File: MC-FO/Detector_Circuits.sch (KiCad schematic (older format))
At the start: 10 parts, among them U141 IFD97, U142 TLV3501AID, U143 74LVC1G32SE-7, U144 74LVC1G0832DBVT

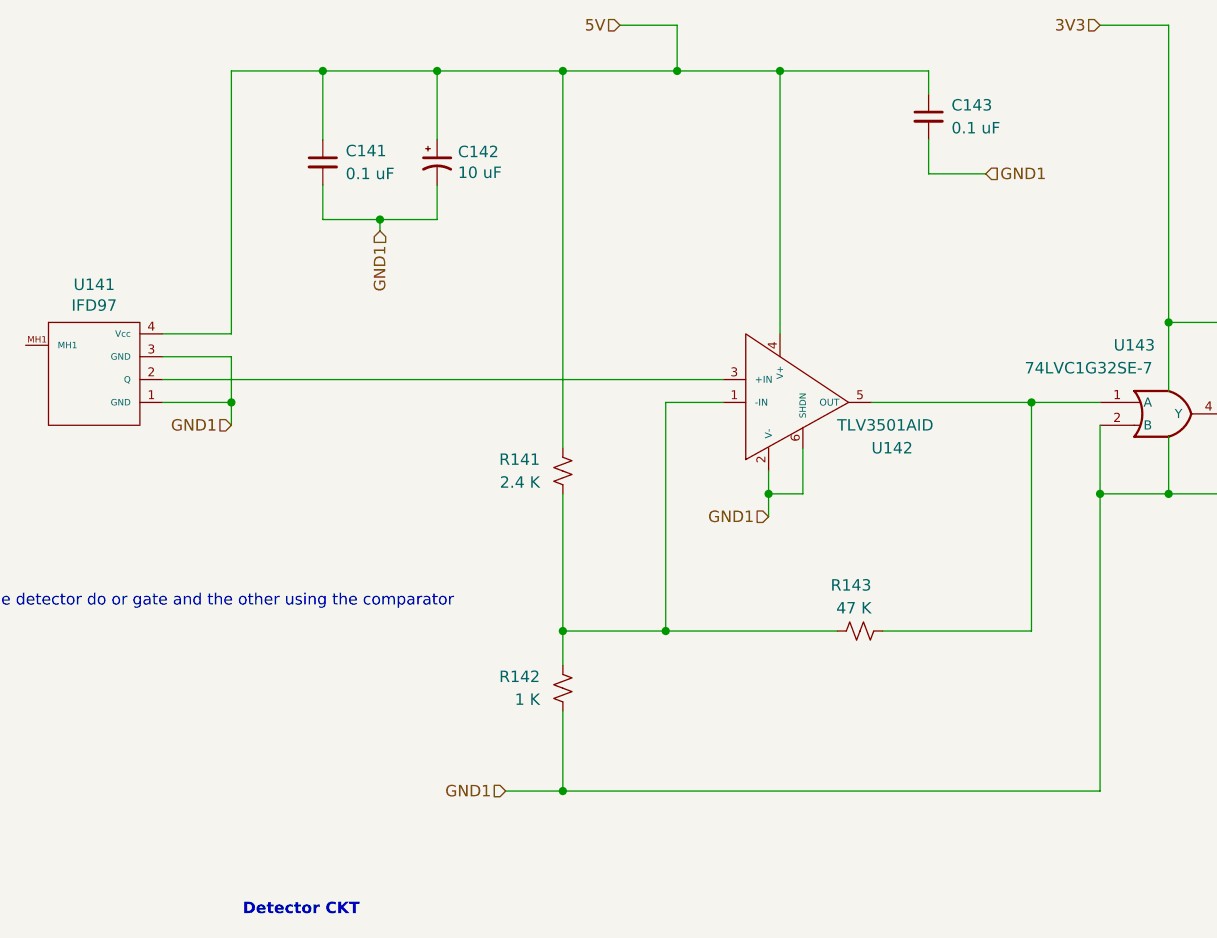
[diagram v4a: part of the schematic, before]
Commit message: changed status1 to output of detector
reassigned footprint of 550 LED
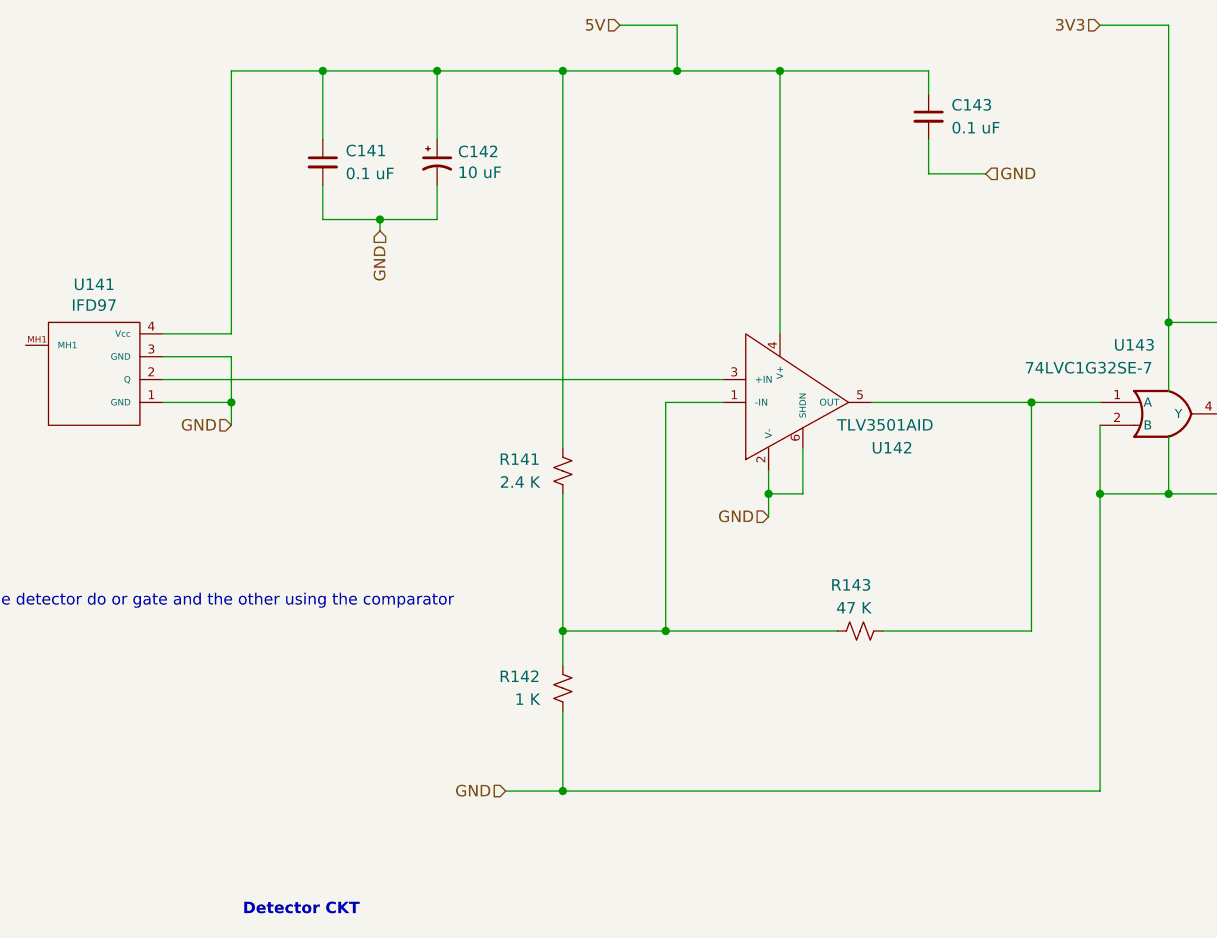
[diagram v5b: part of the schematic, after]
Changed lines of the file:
@@
 Connection ~ 7800 3650
 Text HLabel 5500 5350 0    50   Input ~ 0
-GND1
+GND
 Text HLabel 6650 4150 0    50   Input ~ 0
-GND1
+GND
 Text HLabel 4950 2900 3    50   Input ~ 0
-GND1
+GND
 Text HLabel 4300 3750 0    50   Input ~ 0
-GND1
+GND
 Text HLabel 7600 2650 2    50   Input ~ 0
-GND1
+GND
 Wire Wire Line
 	4700 2850 4950 2850

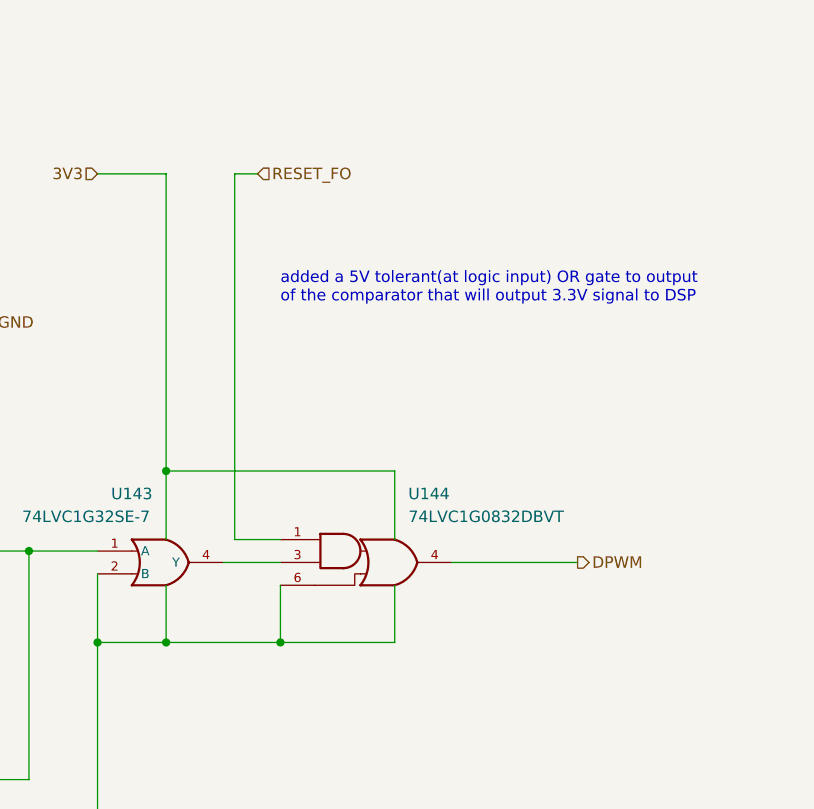
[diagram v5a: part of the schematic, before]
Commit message: Removed AND-OR gates
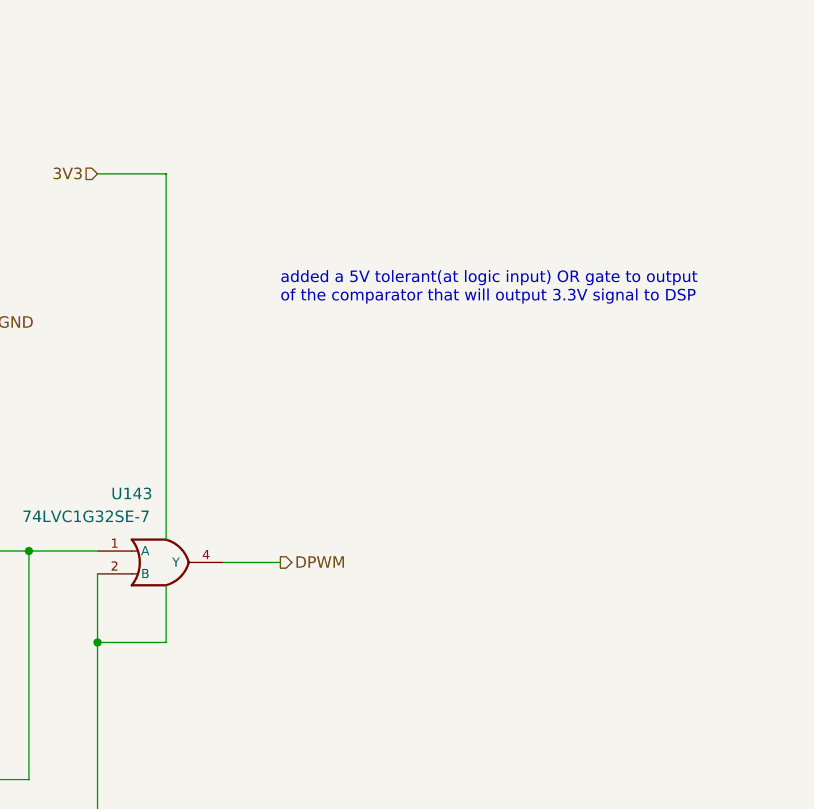
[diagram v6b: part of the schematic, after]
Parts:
- removed U144: 74LVC1G0832DBVT, Package_TO_SOT_SMD:SOT-23-6, symbol Existing_IC_Models:74LVC1G0832DBVT
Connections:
- net DPWM: now also U143.4 (Y)
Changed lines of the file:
@@
 	1    0    0    -1
 $EndComp
-Text HLabel 10200 3700 2    50   Output ~ 0
+Text HLabel 8900 3700 2    50   Output ~ 0
 DPWM
 Text HLabel 6000 2000 0    50   Input ~ 0
@@
 Text Notes 3100 4550 0    50   ~ 0
 on one detector do or gate and the other using the comparator
-Text HLabel 8800 2000 2    50   Input ~ 0
-RESET_FO
 $Comp
 L Existing_IC_Models:74LVC1G32SE-7 U143
@@
 	8100 5350 5750 5350
 Connection ~ 5750 5350
-Wire Wire Line
-	8400 3600 8400 3300
 Text HLabel 8100 2000 0    50   Input ~ 0
 3V3
@@
 added a 5V tolerant(at logic input) OR gate to output\nof the comparator that will output 3.3V signal to DSP\n\n
 Wire Wire Line
-	8800 2000 8700 2000
+	8900 3700 8650 3700
 Wire Wire Line
-	8700 2000 8700 3600
-Wire Wire Line
-	8700 3600 8900 3600
-Wire Wire Line
-	8900 3700 8650 3700
-Connection ~ 8400 3300
-Wire Wire Line
-	8400 3300 8400 2000
-Wire Wire Line
-	9650 3700 10200 3700
-$Comp
-L Existing_IC_Models:74LVC1G0832DBVT U144
-U 1 1 618B7235
-P 9250 3700
-F 0 "U144" H 9550 4000 50  0000 C CNN
-F 1 "74LVC1G0832DBVT" H 9800 3900 50  0000 C CNN
-F 2 "Package_TO_SOT_SMD:SOT-23-6" H 9250 3700 50  0001 C CNN
-F 3 "http://www.ti.com/lit/sg/scyt129e/scyt129e.pdf" H 9250 3700 50  0001 C CNN
-	1    9250 3700
-	1    0    0    -1
-$EndComp
-Connection ~ 8400 4050
-Wire Wire Line
-	9400 3300 9400 3600
-Wire Wire Line
-	8400 3300 9400 3300
-Wire Wire Line
-	8900 4050 8900 3800
-Wire Wire Line
-	8400 4050 8900 4050
-Wire Wire Line
-	8900 4050 9400 4050
-Wire Wire Line
-	9400 4050 9400 3800
-Connection ~ 8900 4050
+	8400 2000 8400 3600
 $EndSCHEMATC

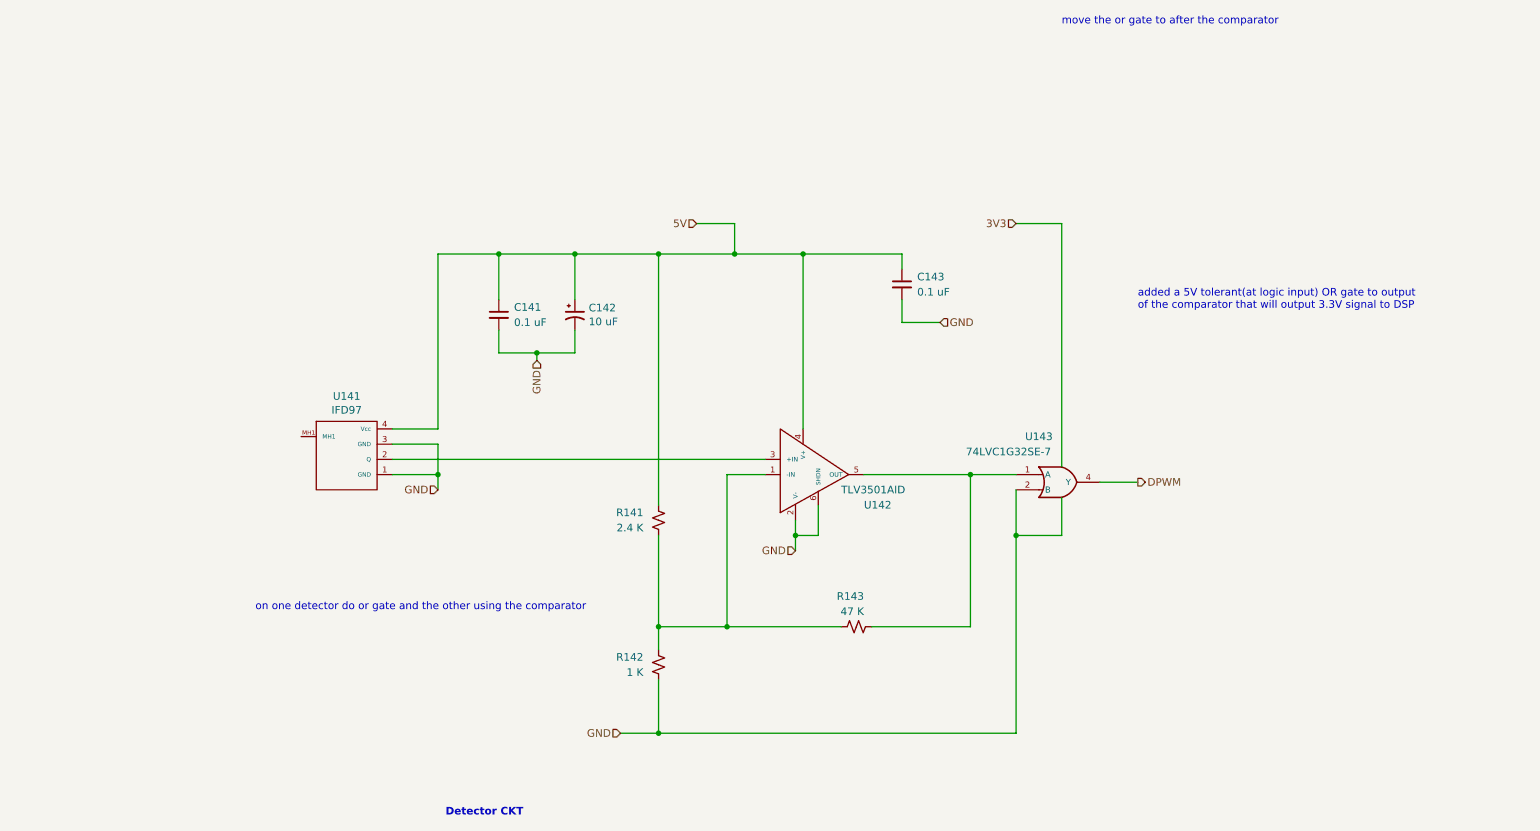
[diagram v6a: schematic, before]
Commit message: DSP schem, FO schem, and FO layout changes
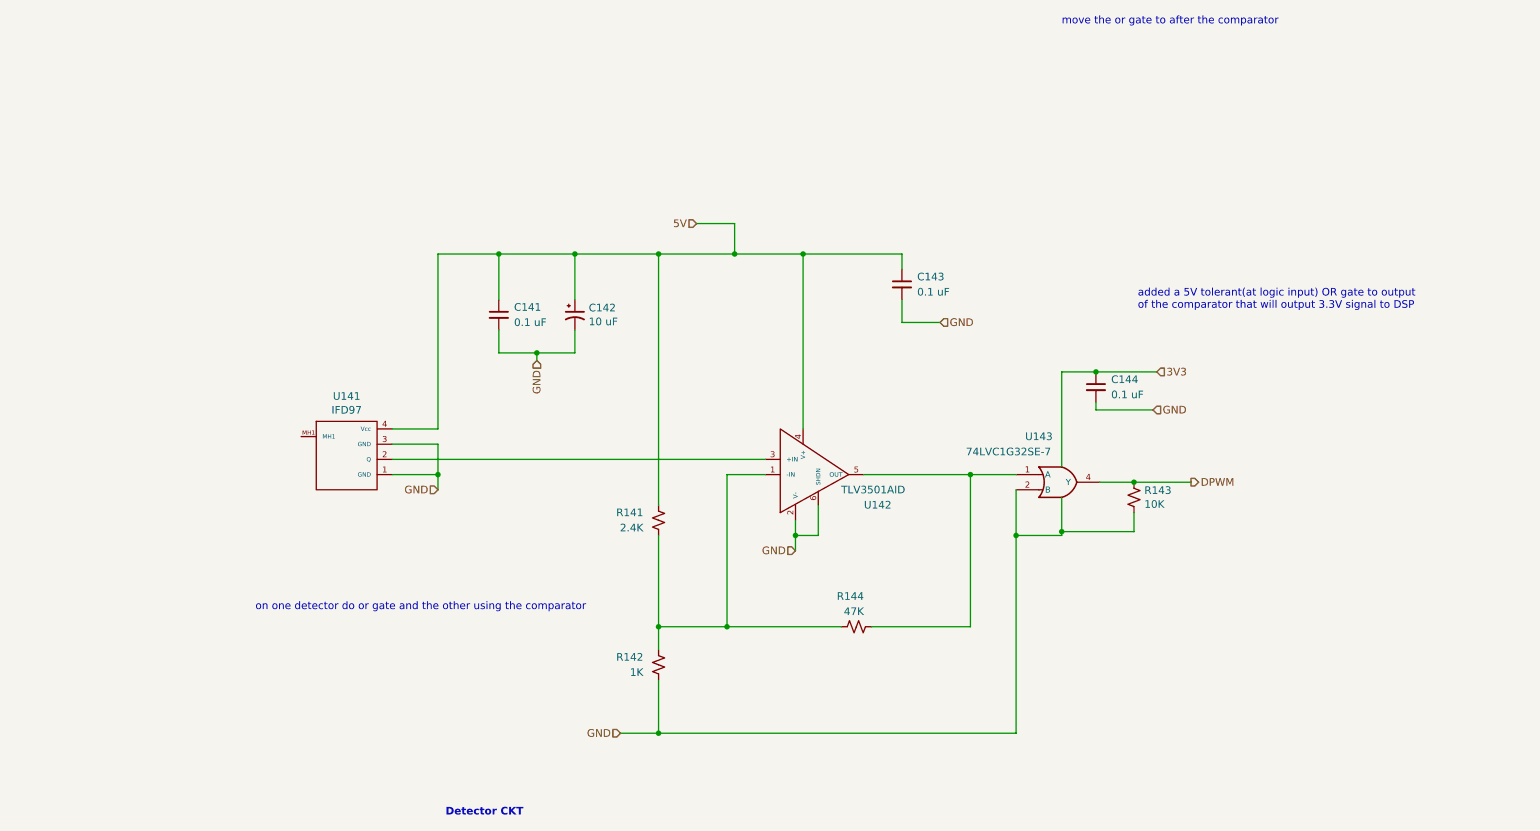
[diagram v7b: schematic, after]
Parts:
- added C144: 0.1 uF, Capacitor_SMD:C_0603_1608Metric, symbol Device:C_Small
- added R143: 10K, Resistor_SMD:R_0603_1608Metric, symbol Device:R_Small_US
- R141: value 2.4 K -> 2.4K
- R142: value 1 K -> 1K
- R144: renamed from R143; value 47 K -> 47K
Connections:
- net DPWM: now also R143.1
- net GND: now also C144.2, R143.2
- net VCC: now also C144.1
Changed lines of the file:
@@
 Detector CKT
-$Comp
-L Device:C_Small C143
-U 1 1 6178E7F5
-P 7350 2400
-AR Path="/6171C819/6178E7F5" Ref="C143"  Part="1"
-AR Path="/61724A08/6178E7F5" Ref="C163"  Part="1"
-F 0 "C143" H 7450 2450 50  0000 L CNN
-F 1 "0.1 uF" H 7450 2350 50  0000 L CNN
-F 2 "Capacitor_SMD:C_0603_1608Metric" H 7350 2400 50  0001 C CNN
-F 3 "~" H 7350 2400 50  0001 C CNN
-	1    7350 2400
-	1    0    0    -1
-$EndComp
-$Comp
-L Device:C_Small C141
-U 1 1 6178E7F6
-P 4700 2600
-AR Path="/6171C819/6178E7F6" Ref="C141"  Part="1"
-AR Path="/61724A08/6178E7F6" Ref="C161"  Part="1"
-F 0 "C141" H 4800 2650 50  0000 L CNN
-F 1 "0.1 uF" H 4800 2550 50  0000 L CNN
-F 2 "Capacitor_SMD:C_0603_1608Metric" H 4700 2600 50  0001 C CNN
-F 3 "~" H 4700 2600 50  0001 C CNN
-	1    4700 2600
-	1    0    0    -1
-$EndComp
 $Comp
 L Device:R_Small_US R141
@@
 AR Path="/61724A08/6174EB5A" Ref="R161"  Part="1"
 F 0 "R141" H 5850 3900 50  0000 L CNN
-F 1 "2.4 K" H 5850 4000 50  0000 L CNN
+F 1 "2.4K" H 5850 4000 50  0000 L CNN
 F 2 "Resistor_SMD:R_0603_1608Metric" H 5750 3950 50  0001 C CNN
 F 3 "~" H 5750 3950 50  0001 C CNN
@@
 	-1   0    0    1
 $EndComp
-$Comp
-L Device:CP1_Small C142
-U 1 1 61720E6A
-P 5200 2600
-AR Path="/6171C819/61720E6A" Ref="C142"  Part="1"
-AR Path="/61724A08/61720E6A" Ref="C162"  Part="1"
-F 0 "C142" H 5291 2646 50  0000 L CNN
-F 1 "10 uF" H 5291 2555 50  0000 L CNN
-F 2 "Capacitor_SMD:C_0603_1608Metric" H 5200 2600 50  0001 C CNN
-F 3 "~" H 5200 2600 50  0001 C CNN
-	1    5200 2600
-	1    0    0    -1
-$EndComp
-Wire Wire Line
-	5200 2850 5200 2700
-Wire Wire Line
-	5200 2500 5200 2200
-Connection ~ 5200 2200
 Wire Wire Line
 	4700 2500 4700 2200
-Wire Wire Line
-	4700 2200 5200 2200
 Wire Wire Line
 	4700 2850 4700 2700
@@
 AR Path="/61724A08/617451F8" Ref="R162"  Part="1"
 F 0 "R142" H 5850 4850 50  0000 L CNN
-F 1 "1 K" H 5850 4950 50  0000 L CNN
+F 1 "1K" H 5850 4950 50  0000 L CNN
 F 2 "Resistor_SMD:R_0603_1608Metric" H 5750 4900 50  0001 C CNN
 F 3 "~" H 5750 4900 50  0001 C CNN
@@
 $EndComp
 $Comp
-L Device:R_Small_US R143
+L Device:R_Small_US R144
 U 1 1 61745A42
 P 7050 4650
-AR Path="/6171C819/61745A42" Ref="R143"  Part="1"
+AR Path="/6171C819/61745A42" Ref="R144"  Part="1"
 AR Path="/61724A08/61745A42" Ref="R163"  Part="1"
-F 0 "R143" V 7250 4600 50  0000 L CNN
-F 1 "47 K" V 7150 4600 50  0000 L CNN
+F 0 "R144" V 7250 4600 50  0000 L CNN
+F 1 "47K" V 7150 4600 50  0000 L CNN
 F 2 "Resistor_SMD:R_0603_1608Metric" H 7050 4650 50  0001 C CNN
 F 3 "~" H 7050 4650 50  0001 C CNN
@@
 	5750 4650 5750 4050
 Connection ~ 5750 4650
-Wire Wire Line
-	5200 2200 5750 2200
-Connection ~ 5750 2200
-Wire Wire Line
-	5750 2200 6250 2200
 Wire Wire Line
 	4700 2200 4300 2200
@@
 	1    0    0    -1
 $EndComp
-Text HLabel 8900 3700 2    50   Output ~ 0
+Text HLabel 9250 3700 2    50   Output ~ 0
 DPWM
 Text HLabel 6000 2000 0    50   Input ~ 0
@@
 Text HLabel 4300 3750 0    50   Input ~ 0
 GND
-Text HLabel 7600 2650 2    50   Input ~ 0
-GND
 Wire Wire Line
 	4700 2850 4950 2850
@@
 Wire Wire Line
 	4950 2850 5200 2850
-Wire Wire Line
-	7350 2500 7350 2650
-Wire Wire Line
-	7350 2200 7350 2300
-Wire Wire Line
-	7350 2650 7600 2650
-Wire Wire Line
-	5750 2200 5750 3850
 Wire Wire Line
 	4000 3550 6450 3550
@@
 $EndComp
 Wire Wire Line
-	6250 2200 6700 2200
-Wire Wire Line
-	6700 2200 6700 3350
-Connection ~ 6700 2200
-Wire Wire Line
-	6700 2200 7350 2200
-Wire Wire Line
 	5750 5000 5750 5350
 Wire Wire Line
@@
 	8100 5350 5750 5350
 Connection ~ 5750 5350
-Text HLabel 8100 2000 0    50   Input ~ 0
+Text HLabel 9025 2975 2    50   Input ~ 0
 3V3
 Wire Wire Line
-	8100 2000 8400 2000
-Wire Wire Line
-	8400 3800 8400 4050
+	9025 2975 8625 2975
+Wire Wire Line
+	8400 3800 8400 4025
 Wire Wire Line
 	8400 4050 8100 4050
@@
 added a 5V tolerant(at logic input) OR gate to output\nof the comparator that will output 3.3V signal to DSP\n\n
 Wire Wire Line
-	8900 3700 8650 3700
-Wire Wire Line
-	8400 2000 8400 3600
+	9250 3700 8875 3700
+Connection ~ 6700 2200
+Wire Wire Line
+	6700 2200 7350 2200
+Wire Wire Line
+	6250 2200 6700 2200
+Wire Wire Line
+	5750 2200 6250 2200
+Connection ~ 5750 2200
+Wire Wire Line
+	5200 2200 5750 2200
+Wire Wire Line
+	4700 2200 5200 2200
+Connection ~ 5200 2200
+Wire Wire Line
+	6700 2200 6700 3350
+Wire Wire Line
+	5750 2200 5750 3850
+Wire Wire Line
+	7350 2650 7600 2650
+Wire Wire Line
+	7350 2200 7350 2300
+Wire Wire Line
+	7350 2500 7350 2650
+Text HLabel 7600 2650 2    50   Input ~ 0
+GND
+Wire Wire Line
+	5200 2500 5200 2200
+Wire Wire Line
+	5200 2850 5200 2700
+$Comp
+L Device:CP1_Small C142
+U 1 1 61720E6A
+P 5200 2600
+AR Path="/6171C819/61720E6A" Ref="C142"  Part="1"
+AR Path="/61724A08/61720E6A" Ref="C162"  Part="1"
+F 0 "C142" H 5291 2646 50  0000 L CNN
+F 1 "10 uF" H 5291 2555 50  0000 L CNN
+F 2 "Capacitor_SMD:C_0603_1608Metric" H 5200 2600 50  0001 C CNN
+F 3 "~" H 5200 2600 50  0001 C CNN
+	1    5200 2600
+	1    0    0    -1
+$EndComp
+$Comp
+L Device:C_Small C141
+U 1 1 6178E7F6
+P 4700 2600
+AR Path="/6171C819/6178E7F6" Ref="C141"  Part="1"
+AR Path="/61724A08/6178E7F6" Ref="C161"  Part="1"
+F 0 "C141" H 4800 2650 50  0000 L CNN
+F 1 "0.1 uF" H 4800 2550 50  0000 L CNN
+F 2 "Capacitor_SMD:C_0603_1608Metric" H 4700 2600 50  0001 C CNN
+F 3 "~" H 4700 2600 50  0001 C CNN
+	1    4700 2600
+	1    0    0    -1
+$EndComp
+$Comp
+L Device:C_Small C143
+U 1 1 6178E7F5
+P 7350 2400
+AR Path="/6171C819/6178E7F5" Ref="C143"  Part="1"
+AR Path="/61724A08/6178E7F5" Ref="C163"  Part="1"
+F 0 "C143" H 7450 2450 50  0000 L CNN
+F 1 "0.1 uF" H 7450 2350 50  0000 L CNN
+F 2 "Capacitor_SMD:C_0603_1608Metric" H 7350 2400 50  0001 C CNN
+F 3 "~" H 7350 2400 50  0001 C CNN
+	1    7350 2400
+	1    0    0    -1
+$EndComp
+$Comp
+L Device:C_Small C144
+U 1 1 618F896A
+P 8625 3075
+AR Path="/6171C819/618F896A" Ref="C144"  Part="1"
+AR Path="/61724A08/618F896A" Ref="C?"  Part="1"
+F 0 "C144" H 8725 3125 50  0000 L CNN
+F 1 "0.1 uF" H 8725 3025 50  0000 L CNN
+F 2 "Capacitor_SMD:C_0603_1608Metric" H 8625 3075 50  0001 C CNN
+F 3 "~" H 8625 3075 50  0001 C CNN
+	1    8625 3075
+	1    0    0    -1
+$EndComp
+Wire Wire Line
+	8400 2975 8400 3600
+Connection ~ 8625 2975
+Wire Wire Line
+	8625 2975 8400 2975
+Text HLabel 9000 3225 2    50   Input ~ 0
+GND
+Wire Wire Line
+	9000 3225 8625 3225
+Wire Wire Line
+	8625 3225 8625 3175
+$Comp
+L Device:R_Small_US R?
+U 1 1 61A62FF1
+P 8875 3800
+AR Path="/61A62FF1" Ref="R?"  Part="1"
+AR Path="/6171C819/61A62FF1" Ref="R143"  Part="1"
+F 0 "R143" H 8943 3846 50  0000 L CNN
+F 1 "10K" H 8943 3755 50  0000 L CNN
+F 2 "Resistor_SMD:R_0603_1608Metric" H 8875 3800 50  0001 C CNN
+F 3 "~" H 8875 3800 50  0001 C CNN
+	1    8875 3800
+	1    0    0    -1
+$EndComp
+Connection ~ 8875 3700
+Wire Wire Line
+	8875 3700 8650 3700
+Wire Wire Line
+	8875 3900 8875 4025
+Wire Wire Line
+	8400 4025 8875 4025
+Connection ~ 8400 4025
+Wire Wire Line
+	8400 4025 8400 4050
 $EndSCHEMATC
